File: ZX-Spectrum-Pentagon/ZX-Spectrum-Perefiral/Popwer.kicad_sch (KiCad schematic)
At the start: 6 parts

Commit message: add keywords for some symbol in library 74IEC update some symbol in zx_custom_symbol improve FDC, Connectors, ZX-Spectrum-Perefiral schematic
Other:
- title: (none) -> ZX-Pentagon-Pereferal
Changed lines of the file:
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@@
 	(generator_version "8.0")
 	(paper "A4")
+	(title_block
+		(title "ZX-Pentagon-Pereferal")
+		(date "2024-03-19")
+		(rev "0.01")
+	)
 	(junction
 		(at 31.75 177.8)

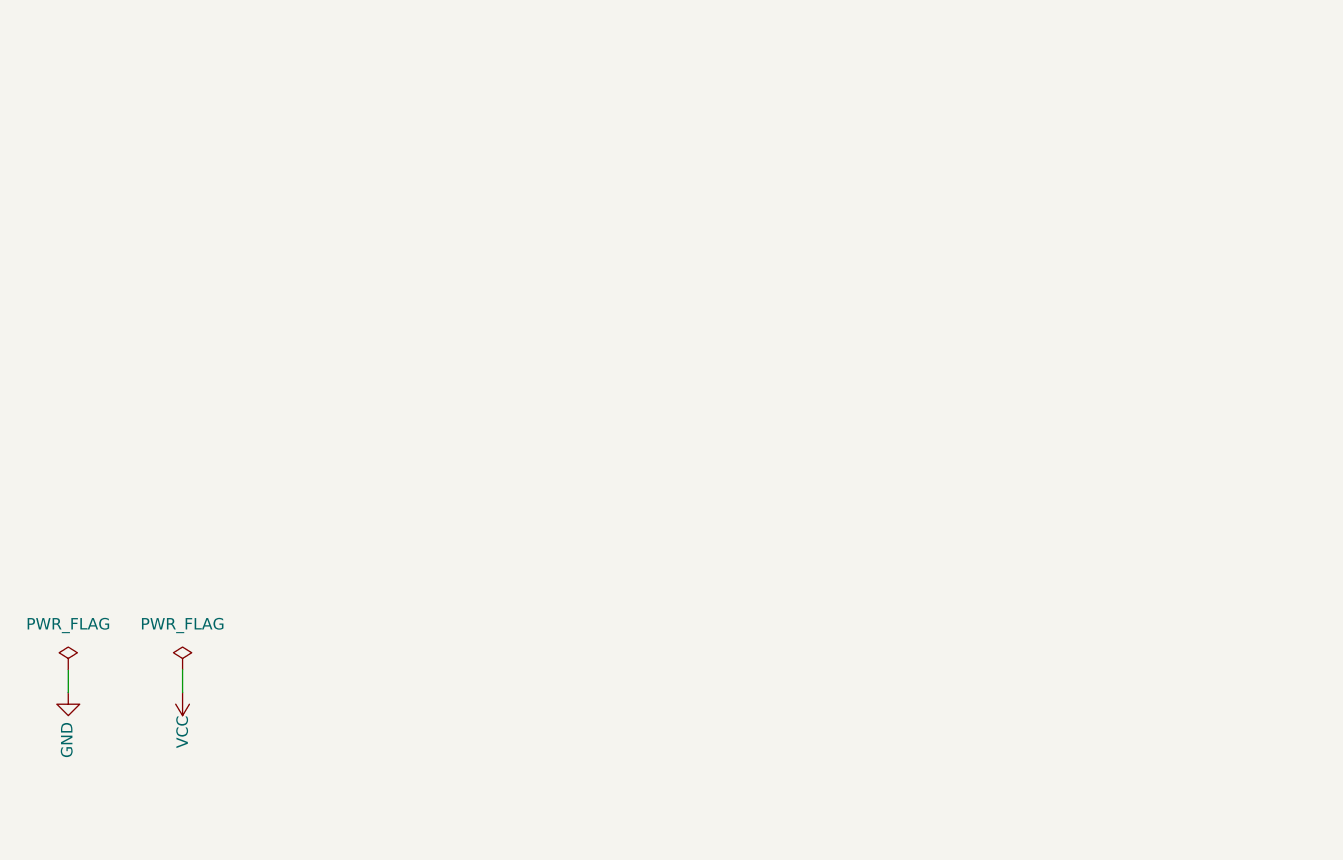
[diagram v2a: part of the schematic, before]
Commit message: fix 74ICE, FDControlers, edge_lib library update all schematic and board fix ERC ZX-Spectrum-Perefiral
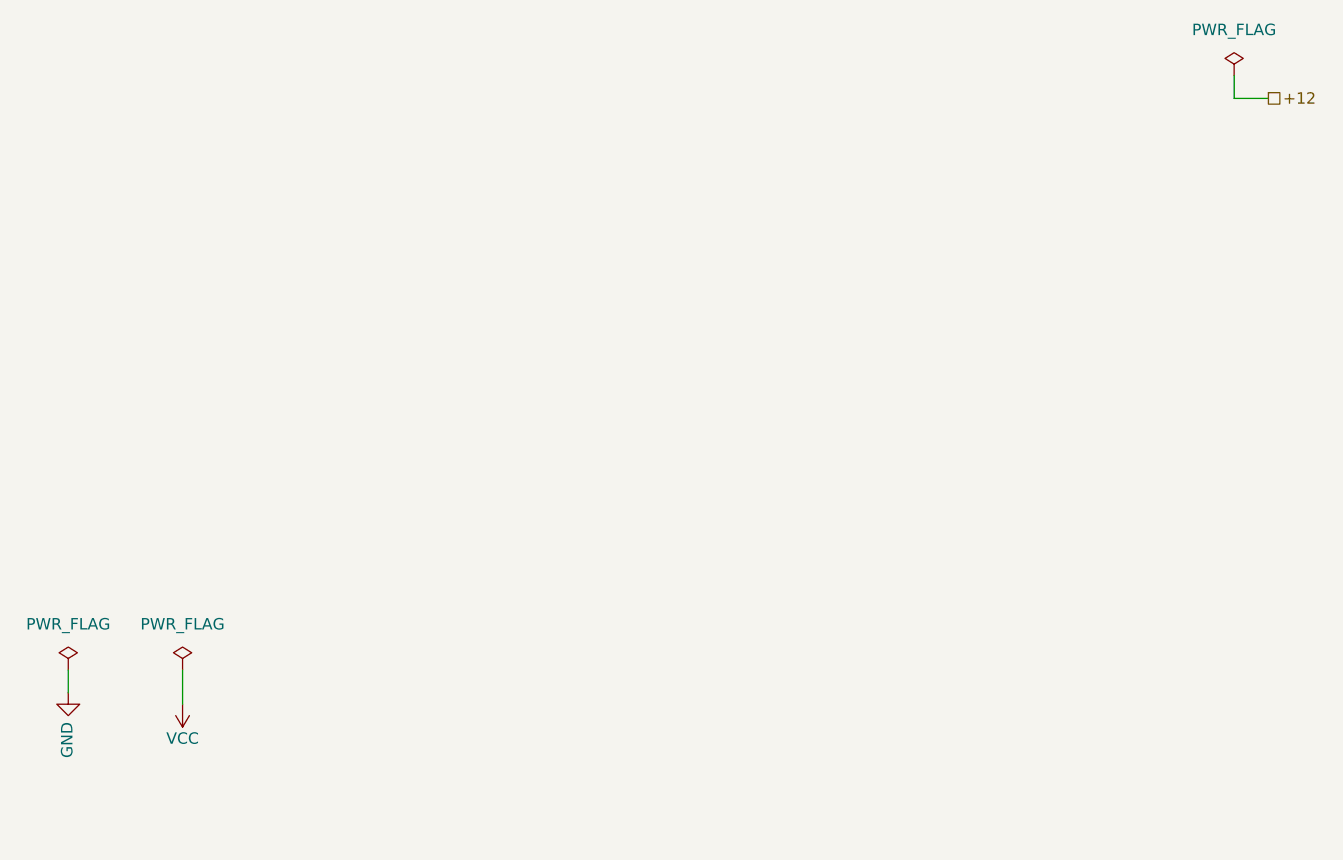
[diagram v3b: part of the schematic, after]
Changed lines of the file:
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@@
+	(wire
+		(pts
+			(xy 111.76 167.64) (xy 111.76 171.45)
+		)
+		(stroke
+			(width 0)
+			(type default)
+		)
+	)
+	(wire
+		(pts
+			(xy 228.6 104.14) (xy 232.41 104.14)
+		)
+		(stroke
+			(width 0)
+			(type default)
+		)
+	)
 	(wire
 		(pts
@@
 	(wire
 		(pts
-			(xy 111.76 167.64) (xy 111.76 170.18)
-		)
-		(stroke
-			(width 0)
-			(type default)
-		)
-	)
-	(wire
-		(pts
 			(xy 50.8 175.26) (xy 50.8 177.8)
 		)
@@
 	(wire
 		(pts
+			(xy 228.6 101.6) (xy 228.6 104.14)
+		)
+		(stroke
+			(width 0)
+			(type default)
+		)
+	)
+	(wire
+		(pts
 			(xy 31.75 175.26) (xy 31.75 177.8)
 		)
@@
 			(width 0)
 			(type default)
+		)
+	)
+	(hierarchical_label "+12"
+		(shape passive)
+		(at 232.41 104.14 0)
+		(fields_autoplaced yes)
+		(effects
+			(font
+				(size 1.27 1.27)
+			)
+			(justify left)
 		)
 	)
@@
 		(dnp no)
 		(fields_autoplaced yes)
-		(property "Reference" "#FLG01"
+		(property "Reference" "#FLG02"
 			(at 99.06 165.735 0)
 			(effects
@@
 			(project "ZX-Spectrum-Perefiral"
 				(path "/b1b48ba2-4f02-4f69-9ca1-50d348cf3e96/da49a933-27e5-4e77-9c00-b924c803c487"
-					(reference "#FLG01")
+					(reference "#FLG02")
 					(unit 1)
 				)
@@
 		(dnp no)
 		(fields_autoplaced yes)
-		(property "Reference" "#PWR028"
+		(property "Reference" "#PWR029"
 			(at 25.4 186.69 0)
 			(effects
@@
 			(project "ZX-Spectrum-Perefiral"
 				(path "/b1b48ba2-4f02-4f69-9ca1-50d348cf3e96/da49a933-27e5-4e77-9c00-b924c803c487"
-					(reference "#PWR028")
+					(reference "#PWR029")
 					(unit 1)
 				)
@@
 				(path "/b1b48ba2-4f02-4f69-9ca1-50d348cf3e96/da49a933-27e5-4e77-9c00-b924c803c487"
 					(reference "H4")
+					(unit 1)
+				)
+			)
+		)
+	)
+	(symbol
+		(lib_id "power:PWR_FLAG")
+		(at 228.6 101.6 0)
+		(unit 1)
+		(exclude_from_sim no)
+		(in_bom yes)
+		(on_board yes)
+		(dnp no)
+		(fields_autoplaced yes)
+		(property "Reference" "#FLG01"
+			(at 228.6 99.695 0)
+			(effects
+				(font
+					(size 1.27 1.27)
+				)
+				(hide yes)
+			)
+		)
+		(property "Value" "PWR_FLAG"
+			(at 228.6 96.52 0)
+			(effects
+				(font
+					(size 1.27 1.27)
+				)
+			)
+		)
+		(property "Footprint" ""
+			(at 228.6 101.6 0)
+			(effects
+				(font
+					(size 1.27 1.27)
+				)
+				(hide yes)
+			)
+		)
+		(property "Datasheet" "~"
+			(at 228.6 101.6 0)
+			(effects
+				(font
+					(size 1.27 1.27)
+				)
+				(hide yes)
+			)
+		)
+		(property "Description" "Special symbol for telling ERC where power comes from"
+			(at 228.6 101.6 0)
+			(effects
+				(font
+					(size 1.27 1.27)
+				)
+				(hide yes)
+			)
+		)
+		(pin "1"
+		)
+		(instances
+			(project "ZX-Spectrum-Perefiral"
+				(path "/b1b48ba2-4f02-4f69-9ca1-50d348cf3e96/da49a933-27e5-4e77-9c00-b924c803c487"
+					(reference "#FLG01")
 					(unit 1)
 				)
@@
 		(on_board yes)
 		(dnp no)
-		(property "Reference" "#PWR026"
+		(property "Reference" "#PWR027"
 			(at 99.06 176.53 0)
 			(effects
@@
 			(project "ZX-Spectrum-Perefiral"
 				(path "/b1b48ba2-4f02-4f69-9ca1-50d348cf3e96/da49a933-27e5-4e77-9c00-b924c803c487"
-					(reference "#PWR026")
+					(reference "#PWR027")
 					(unit 1)
 				)
@@
 	(symbol
 		(lib_id "power:VCC")
-		(at 111.76 170.18 0)
+		(at 111.76 171.45 0)
 		(mirror x)
 		(unit 1)
@@
 		(on_board yes)
 		(dnp no)
-		(property "Reference" "#PWR027"
-			(at 111.76 166.37 0)
+		(property "Reference" "#PWR028"
+			(at 111.76 167.64 0)
 			(effects
 				(font
@@
 		)
 		(property "Value" "VCC"
-			(at 111.76 172.72 90)
-			(effects
-				(font
-					(size 1.27 1.27)
-				)
-				(justify left)
+			(at 111.76 175.26 0)
+			(effects
+				(font
+					(size 1.27 1.27)
+				)
 			)
 		)
 		(property "Footprint" ""
-			(at 111.76 170.18 0)
+			(at 111.76 171.45 0)
 			(effects
 				(font
@@
 		)
 		(property "Datasheet" ""
-			(at 111.76 170.18 0)
+			(at 111.76 171.45 0)
 			(effects
 				(font
@@
 		)
 		(property "Description" "Power symbol creates a global label with name \"VCC\""
-			(at 111.76 170.18 0)
-			(effects
-				(font
-					(size 1.27 1.27)
-				)
-				(hide yes)
-			)
-		)
-		(pin "1"
-		)
-		(instances
-			(project "ZX-Spectrum-Perefiral"
-				(path "/b1b48ba2-4f02-4f69-9ca1-50d348cf3e96/da49a933-27e5-4e77-9c00-b924c803c487"
-					(reference "#PWR027")
+			(at 111.76 171.45 0)
+			(effects
+				(font
+					(size 1.27 1.27)
+				)
+				(hide yes)
+			)
+		)
+		(pin "1"
+		)
+		(instances
+			(project "ZX-Spectrum-Perefiral"
+				(path "/b1b48ba2-4f02-4f69-9ca1-50d348cf3e96/da49a933-27e5-4e77-9c00-b924c803c487"
+					(reference "#PWR028")
 					(unit 1)
 				)
@@
 		(dnp no)
 		(fields_autoplaced yes)
-		(property "Reference" "#FLG02"
+		(property "Reference" "#FLG03"
 			(at 111.76 165.735 0)
 			(effects
@@
 			(project "ZX-Spectrum-Perefiral"
 				(path "/b1b48ba2-4f02-4f69-9ca1-50d348cf3e96/da49a933-27e5-4e77-9c00-b924c803c487"
-					(reference "#FLG02")
-					(unit 1)
-				)
+					(reference "#FLG03")
+					(unit 1)
+				)

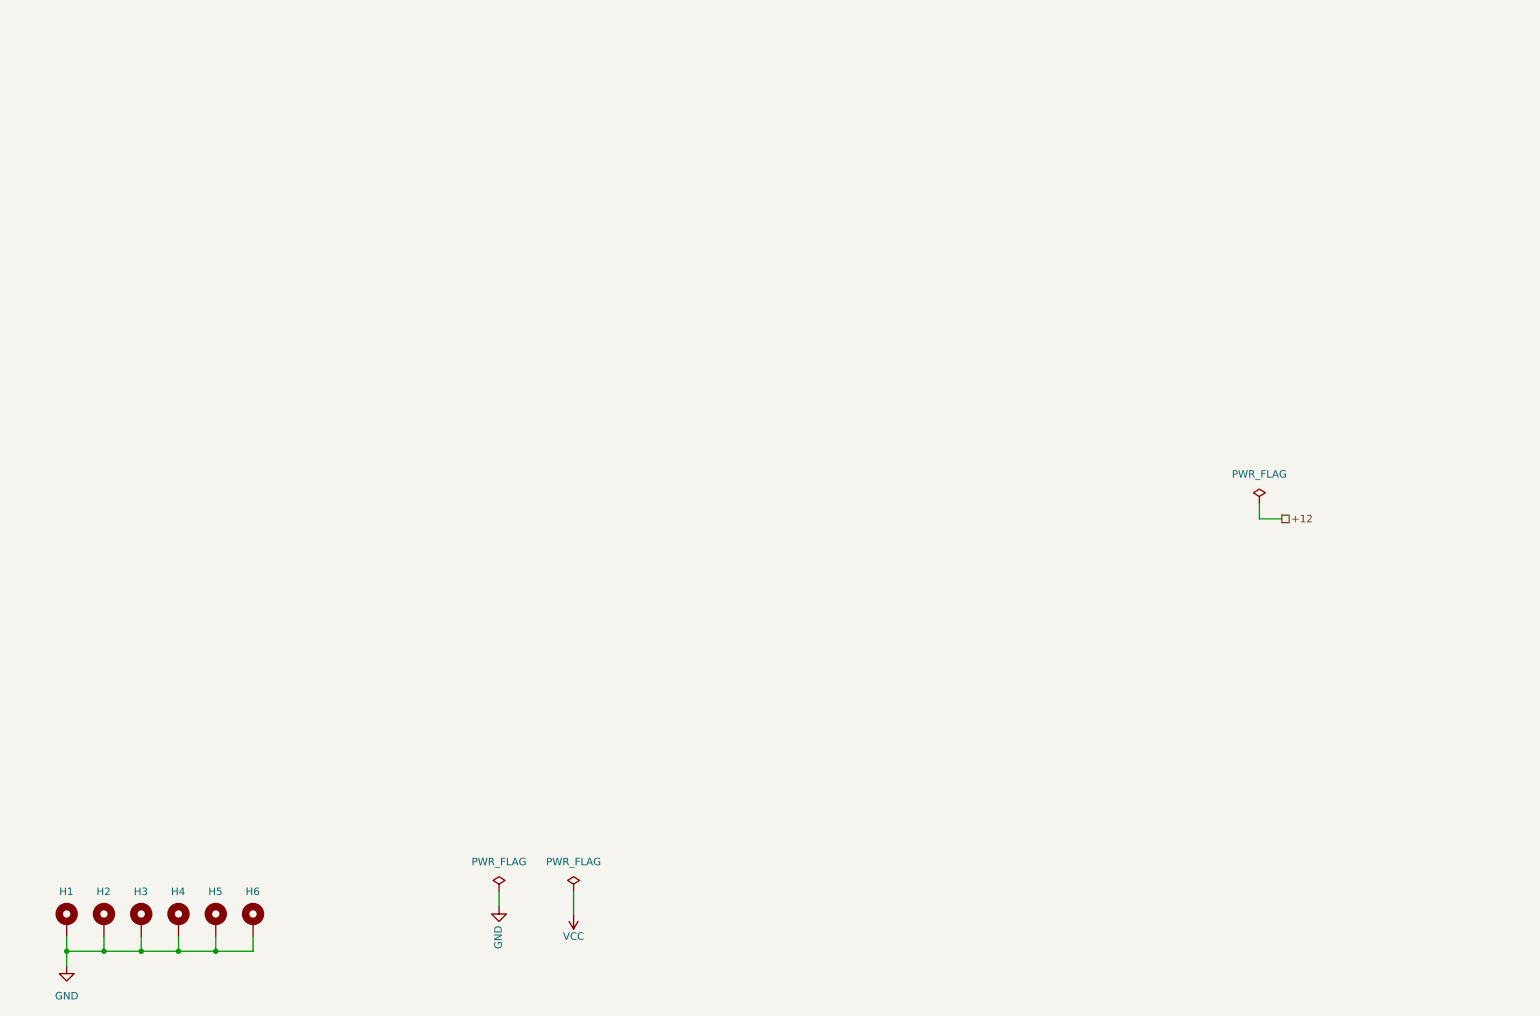
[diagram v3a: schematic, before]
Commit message: FDControlers rename from VCC1 to VDD zx_custom_symbol add connector Conn_02x32_Odd_Even ZX-Spectrum-Pentagon rename from +9V to POWER ZX-Spectrum-Perefiral improve schematic
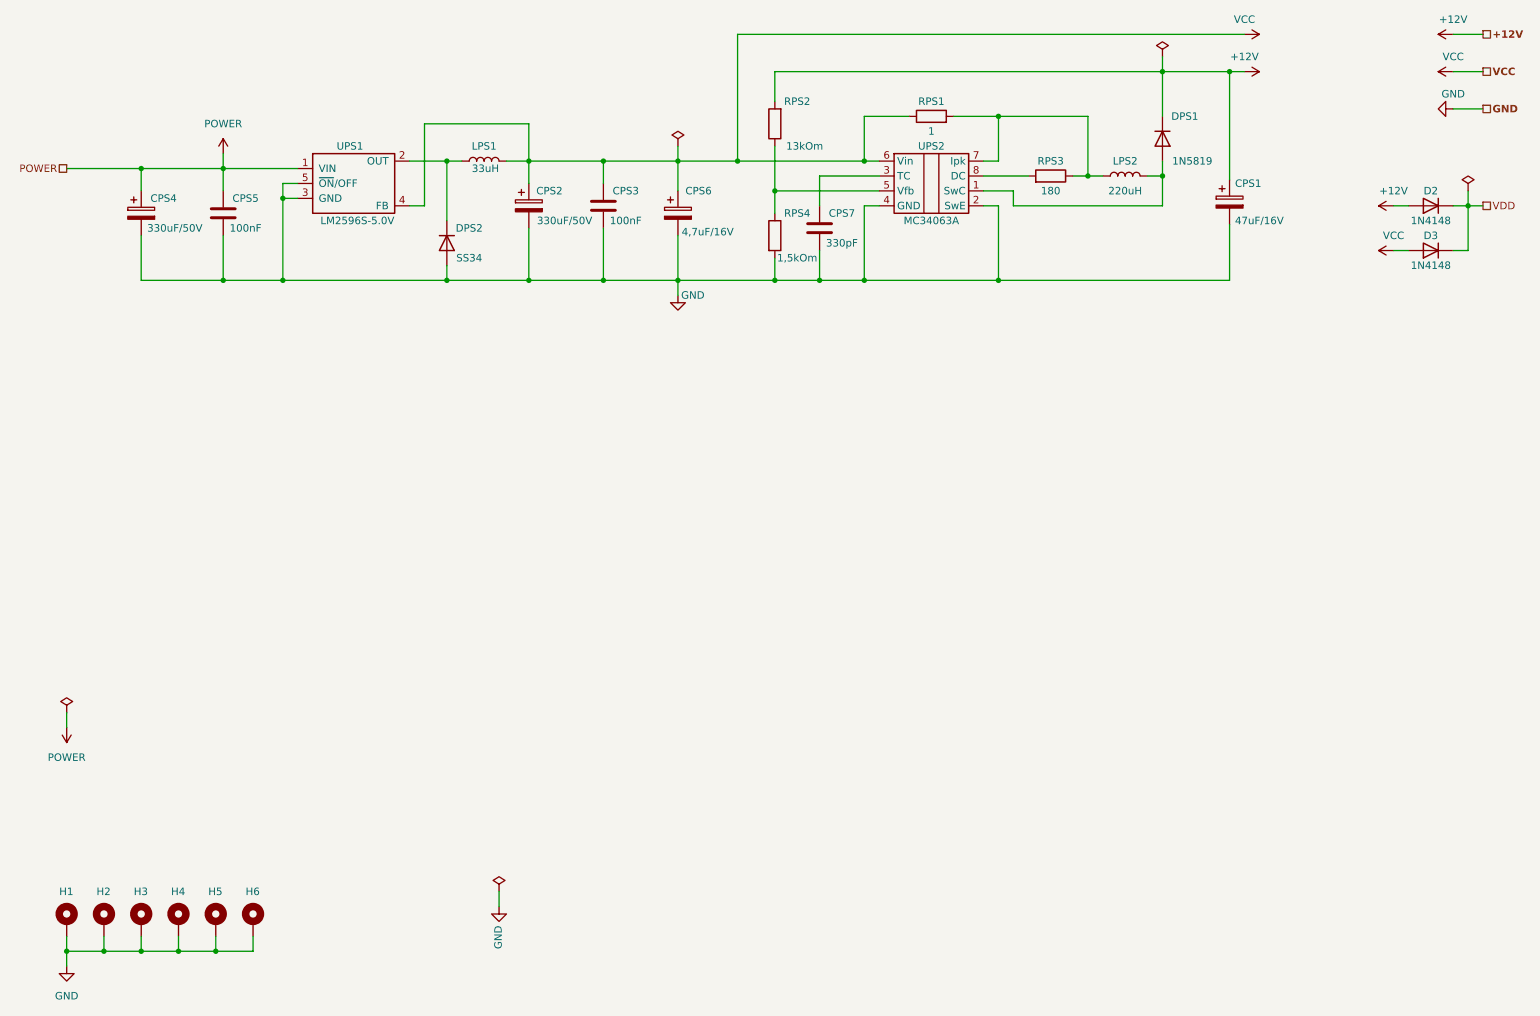
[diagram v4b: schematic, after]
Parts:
- added CPS1: 47uF/16V, Capacitor_Tantalum_SMD:CP_EIA-3216-18_Kemet-A_Pad1.58x1.35mm_HandSolder, symbol Device:C_Polarized
- added CPS2, CPS4: 330uF/50V, Capacitor_Tantalum_SMD:CP_EIA-7343-31_Kemet-D_Pad2.25x2.55mm_HandSolder, symbol Device:C_Polarized
- added CPS3, CPS5: 100nF, Capacitor_SMD:C_0805_2012Metric_Pad1.18x1.45mm_HandSolder, symbol Device:C
- added CPS6: 4,7uF/16V, Capacitor_Tantalum_SMD:CP_EIA-3216-18_Kemet-A_Pad1.58x1.35mm_HandSolder, symbol Device:C_Polarized
- added CPS7: 330pF, Capacitor_SMD:C_0805_2012Metric_Pad1.18x1.45mm_HandSolder, symbol Device:C
- added D2, D3: 1N4148, Diode_SMD:D_MiniMELF, symbol Device:D
- added DPS1: 1N5819, Diode_SMD:D_SOD-323_HandSoldering, symbol Device:D
- added DPS2: SS34, Diode_SMD:D_SMA, symbol Device:D
- added LPS1: 33uH, Inductor_SMD:L_12x12mm_H6mm, symbol Device:L
- added LPS2: 220uH, CDInductor:CD43, symbol Device:L
- added RPS1: 1, Resistor_SMD:R_0805_2012Metric_Pad1.20x1.40mm_HandSolder, symbol Device:R
- added RPS2: 13kOm, Resistor_SMD:R_0805_2012Metric_Pad1.20x1.40mm_HandSolder, symbol Device:R
- added RPS3: 180, Resistor_SMD:R_0805_2012Metric_Pad1.20x1.40mm_HandSolder, symbol Device:R
- added RPS4: 1,5kOm, Resistor_SMD:R_0805_2012Metric_Pad1.20x1.40mm_HandSolder, symbol Device:R
- added UPS1: LM2596S-5.0V, Package_TO_SOT_SMD:TO-263-5_TabPin3, symbol zx_custom_symbol:LM2596S-5.0V
- added UPS2: MC34063A, Package_SO:SO-8_3.9x4.9mm_P1.27mm, symbol zx_custom_symbol:MC34063A
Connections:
- net GND: now also CPS1.2, CPS2.2, CPS3.2, CPS4.2, CPS5.2, CPS6.2, CPS7.2, DPS2.2 (A), RPS4.2, UPS1.3 (GND), UPS1.5 (~{ON}/OFF), UPS2.2 (SwE), UPS2.4 (GND)
- net VCC: now also CPS2.1, CPS3.1, CPS6.1, D3.2 (A), LPS1.2, RPS1.1, UPS1.4 (FB), UPS2.6 (Vin)
- new net: DPS1.2 (A), LPS2.1, UPS2.1 (SwC)
- new net: CPS7.1, UPS2.3 (TC)
- new net: RPS2.1, RPS4.1, UPS2.5 (Vfb)
- new net: LPS2.2, RPS1.2, RPS3.1, UPS2.7 (Ipk)
- new net: RPS3.2, UPS2.8 (DC)
- new net: DPS2.1 (K), LPS1.1, UPS1.2 (OUT)
- new net +12V: CPS1.1, D2.2 (A), DPS1.1 (K), RPS2.2
- new net POWER: CPS4.1, CPS5.1, UPS1.1 (VIN)
- new net VDD: D2.1 (K), D3.1 (K)
